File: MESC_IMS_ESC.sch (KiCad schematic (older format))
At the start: 58 parts, among them J1 Conn_01x08_Female, J2 Conn_01x08_Female, J3 Conn_01x08_Female, J4 Conn_01x06_Male, J5 Conn_ARM_JTAG_SWD_10, J6 USB_C_Receptacle_USB2.0, J7 Conn_01x03_Male, J8 Conn_01x04_Male, J9 Conn_01x08_Male, U1 STM32F303CBTx, Y1 ASE-8.000MHZ-LC-T

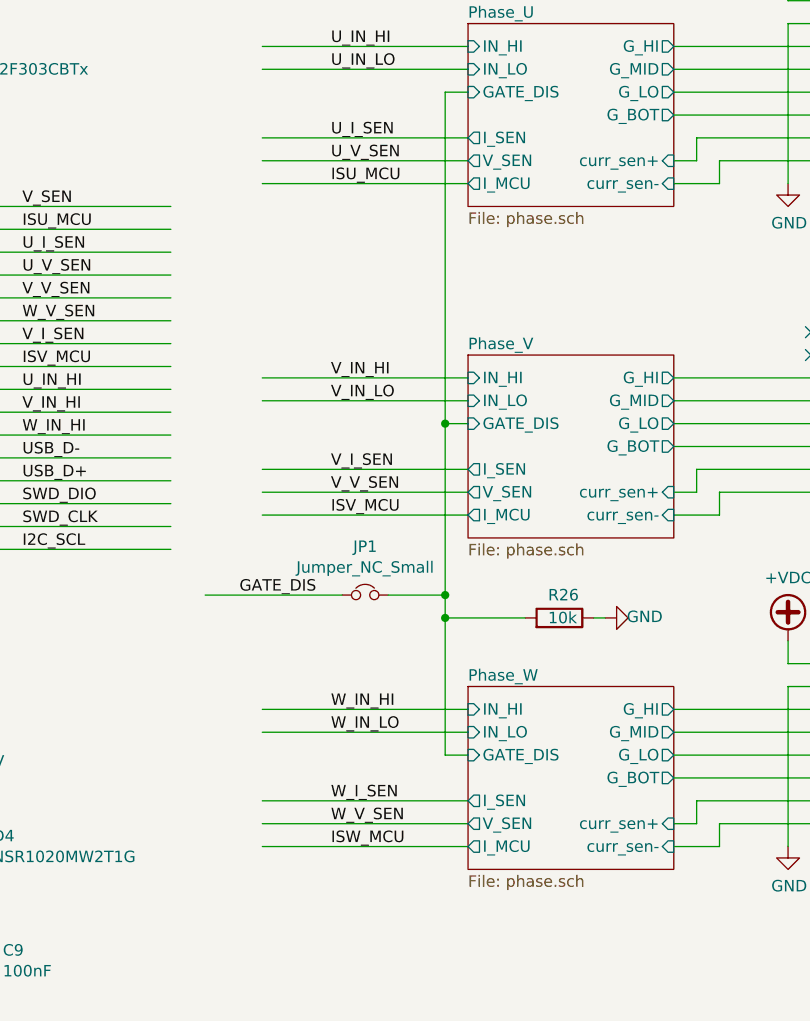
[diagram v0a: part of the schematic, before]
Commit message: Minor updates
Tweaking the README.md
Removing F303 op-amp circuitry.
Re-arranging INA240 circuit
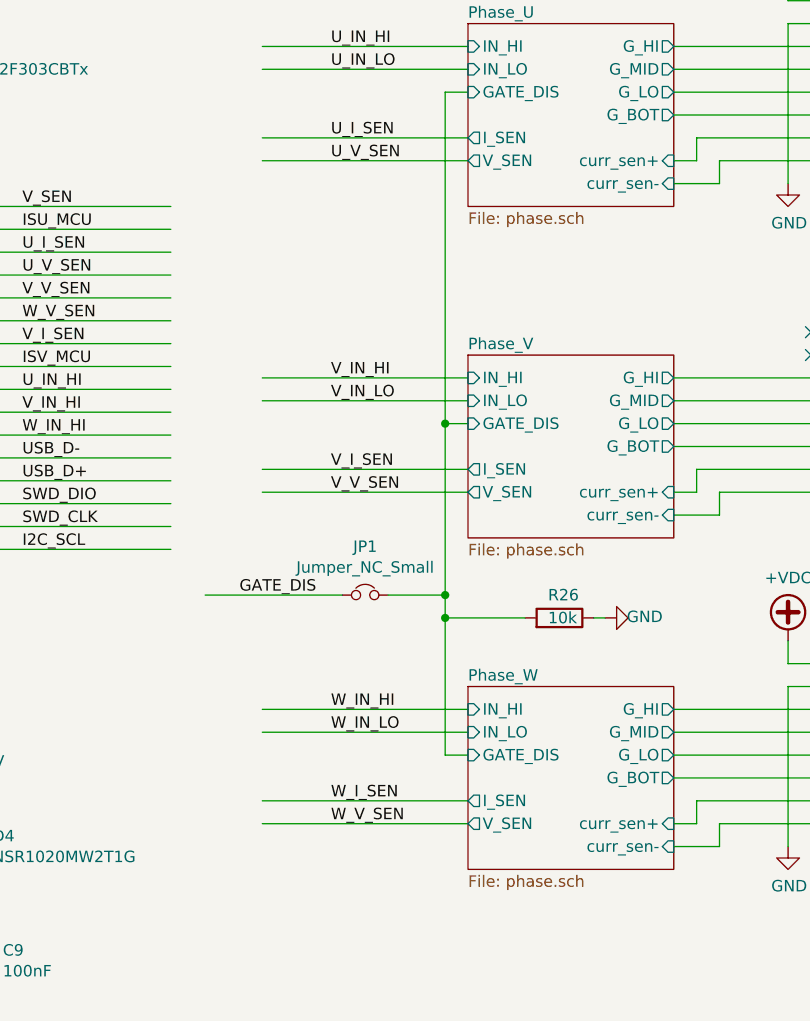
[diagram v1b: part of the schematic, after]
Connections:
- wire segments 279 -> 276
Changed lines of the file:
@@
 F11 "G_BOT" O R 9550 2950 50
 F12 "GATE_DIS" I L 8650 2850 50
-F13 "I_MCU" O L 8650 3250 50
 $EndSheet
 $Sheet
@@
 F11 "G_BOT" O R 9550 4400 50
 F12 "GATE_DIS" I L 8650 4300 50
-F13 "I_MCU" O L 8650 4700 50
 $EndSheet
 $Sheet
@@
 F11 "G_BOT" O R 9550 5850 50
 F12 "GATE_DIS" I L 8650 5750 50
-F13 "I_MCU" O L 8650 6150 50
 $EndSheet
 Wire Wire Line
@@
 	10050 2250 10050 2350
 Wire Wire Line
-	8650 3250 7750 3250
-Text Label 8050 3250 0    50   ~ 0
-ISU_MCU
-Wire Wire Line
 	5150 3850 4250 3850
 Text Label 4500 3850 0    50   ~ 0
 GATE_DIS
 Wire Wire Line
-	8650 4700 7750 4700
-Text Label 8050 4700 0    50   ~ 0
-ISV_MCU
-Wire Wire Line
-	8650 6150 7750 6150
-Text Label 8050 6150 0    50   ~ 0
-ISW_MCU
-Wire Wire Line
 	8650 2850 8550 2850

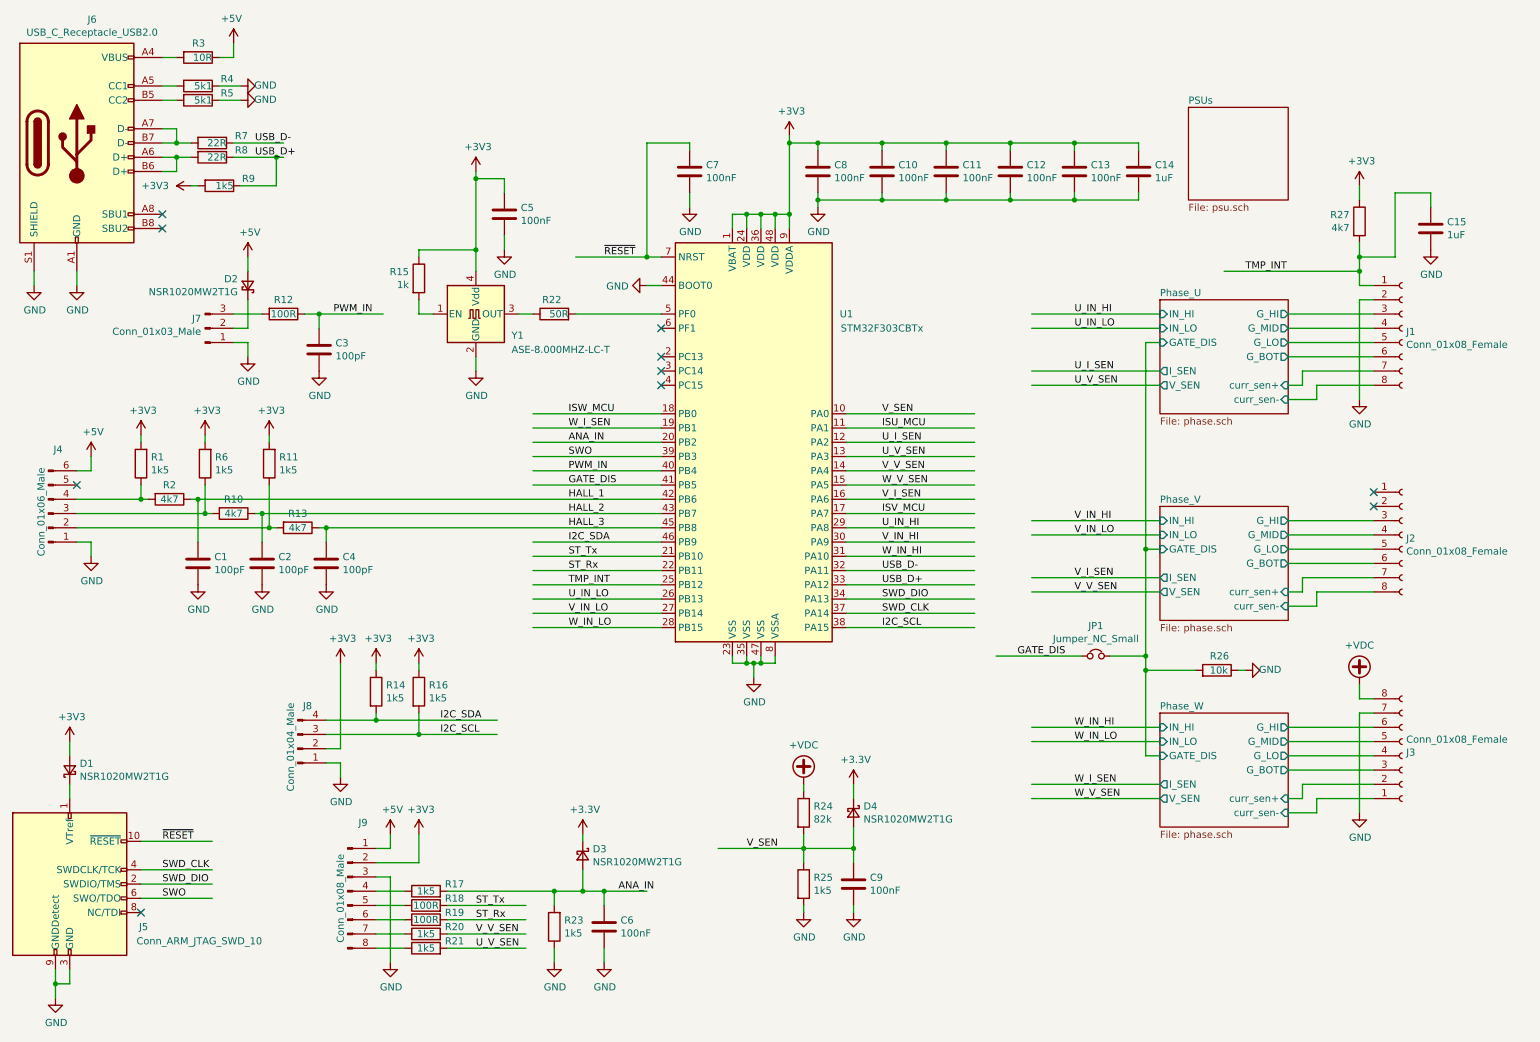
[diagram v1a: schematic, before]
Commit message: Adding some test points
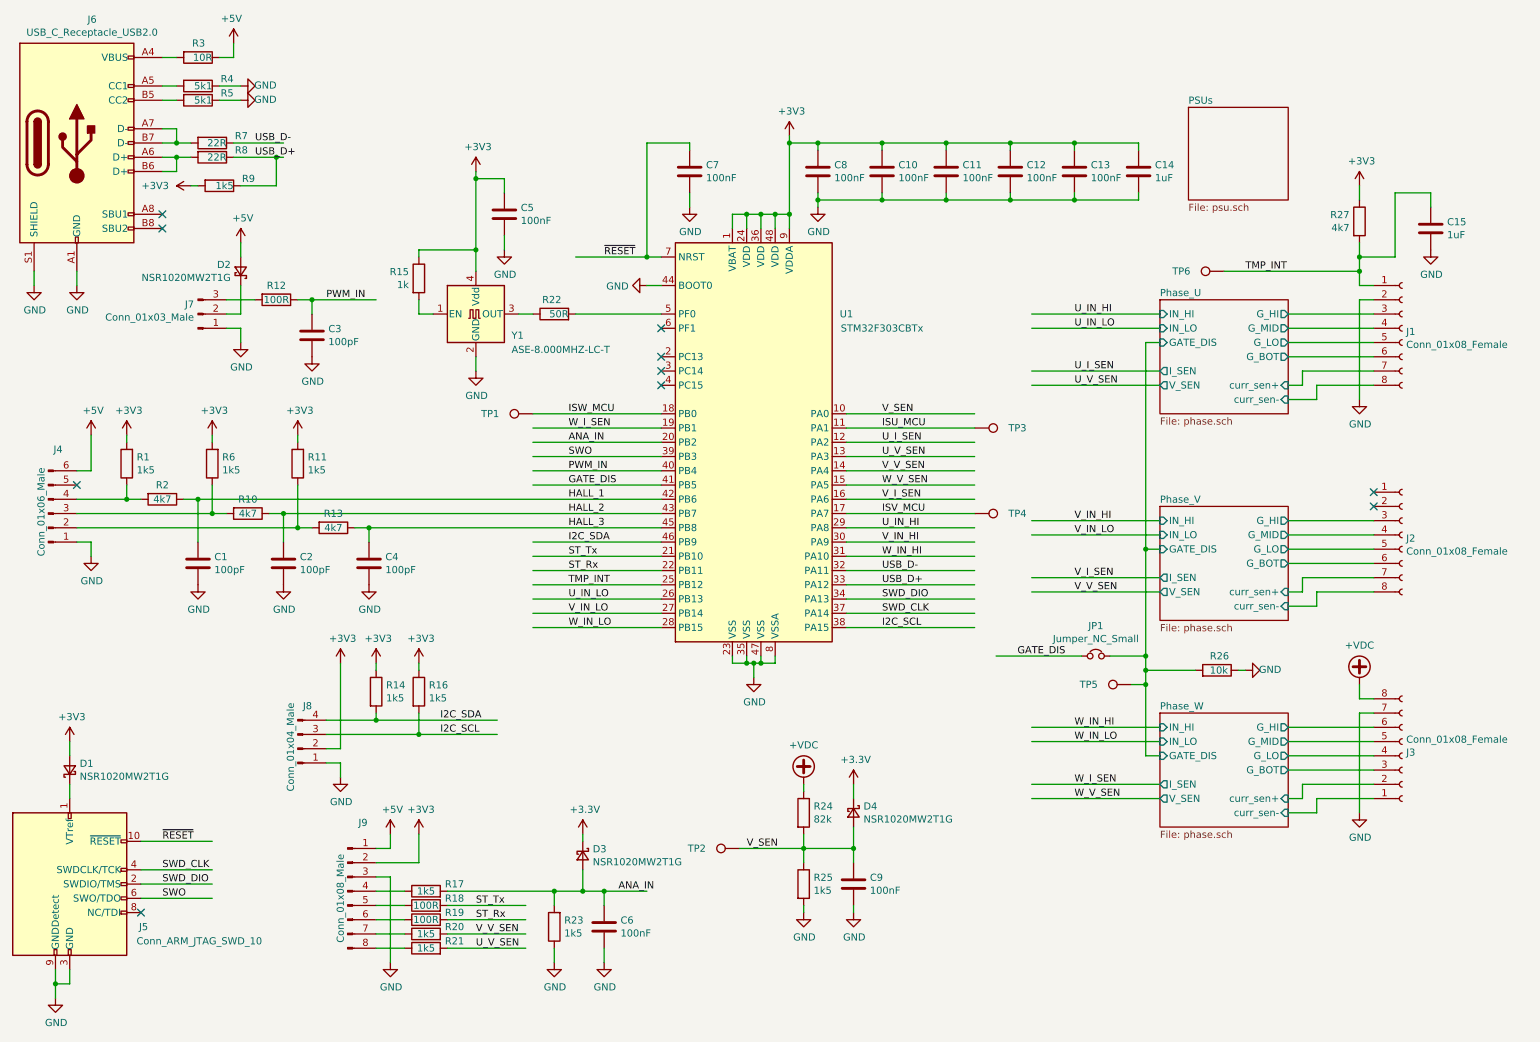
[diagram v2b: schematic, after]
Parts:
- added TP1, TP2, TP3, TP4, TP5, TP6: TestPoint, symbol Connector:TestPoint
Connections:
- wire segments 276 -> 278
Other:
- moved on the sheet: C2, C3, C4, D2, J7, R1, R10, R11, R12, R13, R2, R6

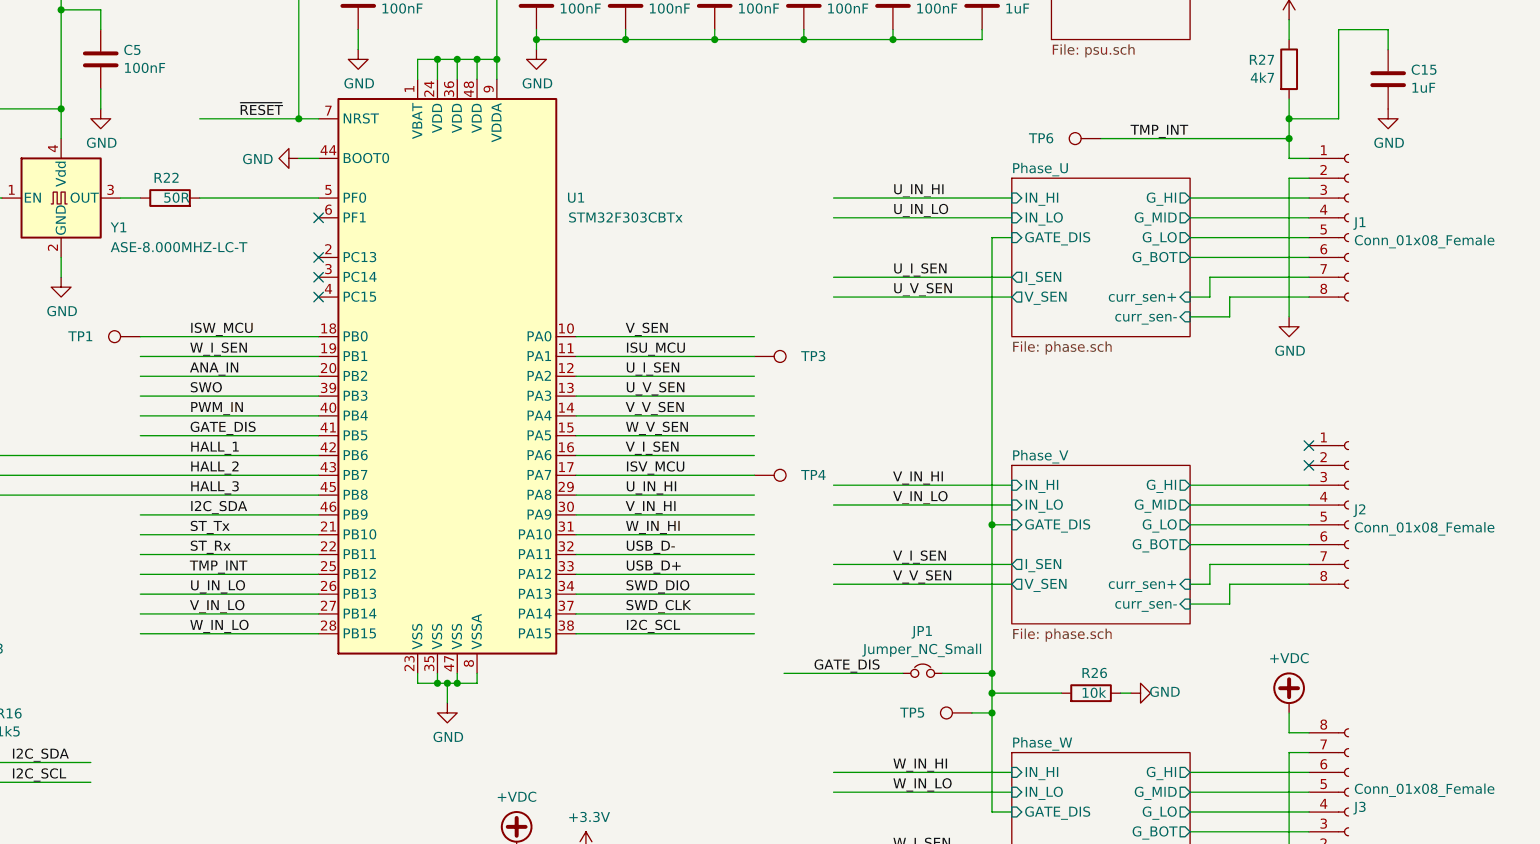
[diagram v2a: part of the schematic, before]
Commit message: Assigned all footprints
Began initial placement
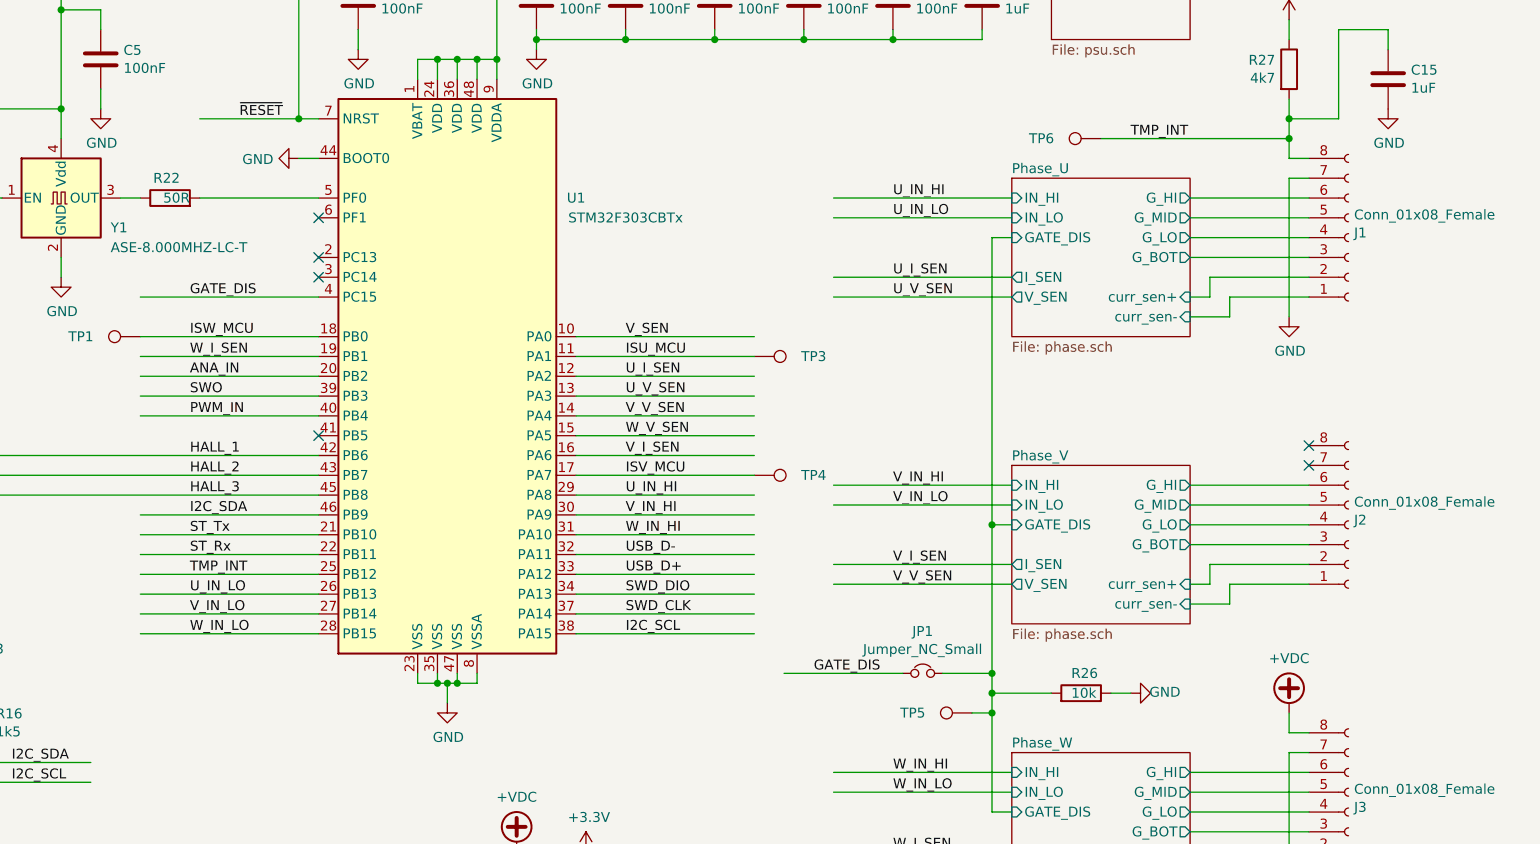
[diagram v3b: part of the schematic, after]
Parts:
- C14: footprint (none) -> Capacitor_SMD:C_0402_1005Metric
- TP1, TP2, TP3, TP4, TP5, TP6: footprint (none) -> TestPoint:TestPoint_Pad_D1.5mm
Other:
- moved on the sheet: R26
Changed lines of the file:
@@
 L Connector:Conn_01x08_Female J1
 U 1 1 607F595D
-P 10350 2750
-F 0 "J1" H 10378 2726 50  0000 L CNN
-F 1 "Conn_01x08_Female" H 10378 2635 50  0000 L CNN
-F 2 "Connector_PinSocket_2.54mm:PinSocket_1x08_P2.54mm_Horizontal" H 10350 2750 50  0001 C CNN
-F 3 "~" H 10350 2750 50  0001 C CNN
-	1    10350 2750
-	1    0    0    -1
+P 10350 2850
+F 0 "J1" H 10378 2826 50  0000 L CNN
+F 1 "Conn_01x08_Female" H 10378 2735 50  0000 L CNN
+F 2 "Connector_PinSocket_2.54mm:PinSocket_1x08_P2.54mm_Horizontal" H 10350 2850 50  0001 C CNN
+F 3 "~" H 10350 2850 50  0001 C CNN
+	1    10350 2850
+	1    0    0    1
 $EndComp
 $Comp
 L Connector:Conn_01x08_Female J2
 U 1 1 607F7758
-P 10350 4200
-F 0 "J2" H 10378 4176 50  0000 L CNN
-F 1 "Conn_01x08_Female" H 10378 4085 50  0000 L CNN
-F 2 "Connector_PinSocket_2.54mm:PinSocket_1x08_P2.54mm_Horizontal" H 10350 4200 50  0001 C CNN
-F 3 "~" H 10350 4200 50  0001 C CNN
-	1    10350 4200
-	1    0    0    -1
+P 10350 4300
+F 0 "J2" H 10378 4276 50  0000 L CNN
+F 1 "Conn_01x08_Female" H 10378 4185 50  0000 L CNN
+F 2 "Connector_PinSocket_2.54mm:PinSocket_1x08_P2.54mm_Horizontal" H 10350 4300 50  0001 C CNN
+F 3 "~" H 10350 4300 50  0001 C CNN
+	1    10350 4300
+	1    0    0    1
 $EndComp
 $Comp
@@
 NoConn ~ 5150 2950
 NoConn ~ 5150 3050
-NoConn ~ 5150 3150
 NoConn ~ 1500 6850
 Wire Wire Line
@@
 F 0 "C14" H 8615 1696 50  0000 L CNN
 F 1 "1uF" H 8615 1605 50  0000 L CNN
-F 2 "" H 8538 1500 50  0001 C CNN
+F 2 "Capacitor_SMD:C_0402_1005Metric" H 8538 1500 50  0001 C CNN
 F 3 "~" H 8500 1650 50  0001 C CNN
 	1    8500 1650
@@
 	10050 2250 10050 2350
 Wire Wire Line
-	5150 3850 4250 3850
-Text Label 4500 3850 0    50   ~ 0
+	5150 3150 4250 3150
+Text Label 4500 3150 0    50   ~ 0
 GATE_DIS
 Wire Wire Line
@@
 $EndComp
 Wire Wire Line
-	9200 5150 9250 5150
+	9150 5150 9250 5150
 $Comp
 L Device:R R?
 U 1 1 61980155
-P 9050 5150
+P 9000 5150
 AR Path="/6070CE7F/61980155" Ref="R?"  Part="1"
 AR Path="/6074FE4E/61980155" Ref="R?"  Part="1"
 AR Path="/6075047A/61980155" Ref="R?"  Part="1"
 AR Path="/61980155" Ref="R26"  Part="1"
-F 0 "R26" V 9150 5100 50  0000 L CNN
-F 1 "10k" V 9050 5100 50  0000 L CNN
-F 2 "Resistor_SMD:R_0402_1005Metric" V 8980 5150 50  0001 C CNN
-F 3 "~" H 9050 5150 50  0001 C CNN
-	1    9050 5150
+F 0 "R26" V 9100 5100 50  0000 L CNN
+F 1 "10k" V 9000 5100 50  0000 L CNN
+F 2 "Resistor_SMD:R_0402_1005Metric" V 8930 5150 50  0001 C CNN
+F 3 "~" H 9000 5150 50  0001 C CNN
+	1    9000 5150
 	0    1    -1   0
 $EndComp
@@
 	8550 4300 8550 5050
 Wire Wire Line
-	8900 5150 8550 5150
+	8850 5150 8550 5150
 Wire Wire Line
 	8550 2850 8550 4300
@@
 F 0 "TP1" V 4250 3650 50  0000 C CNN
 F 1 "TestPoint" V 4354 3422 50  0001 C CNN
-F 2 "" H 4450 3350 50  0001 C CNN
+F 2 "TestPoint:TestPoint_Pad_D1.5mm" H 4450 3350 50  0001 C CNN
 F 3 "~" H 4450 3350 50  0001 C CNN
 	1    4250 3350
@@
 F 0 "TP3" V 7350 3750 50  0000 C CNN
 F 1 "TestPoint" V 7454 3522 50  0001 C CNN
-F 2 "" H 7550 3450 50  0001 C CNN
+F 2 "TestPoint:TestPoint_Pad_D1.5mm" H 7550 3450 50  0001 C CNN
 F 3 "~" H 7550 3450 50  0001 C CNN
 	1    7350 3450
@@
 F 0 "TP4" V 7350 4350 50  0000 C CNN
 F 1 "TestPoint" V 7454 4122 50  0001 C CNN
-F 2 "" H 7550 4050 50  0001 C CNN
+F 2 "TestPoint:TestPoint_Pad_D1.5mm" H 7550 4050 50  0001 C CNN
 F 3 "~" H 7550 4050 50  0001 C CNN
 	1    7350 4050
@@
 F 0 "TP6" V 9100 2650 50  0000 C CNN
 F 1 "TestPoint" V 9204 2422 50  0001 C CNN
-F 2 "" H 9300 2350 50  0001 C CNN
+F 2 "TestPoint:TestPoint_Pad_D1.5mm" H 9300 2350 50  0001 C CNN
 F 3 "~" H 9300 2350 50  0001 C CNN
 	1    9100 2350
@@
 F 0 "TP2" V 5700 6700 50  0000 C CNN
 F 1 "TestPoint" V 5804 6472 50  0001 C CNN
-F 2 "" H 5900 6400 50  0001 C CNN
+F 2 "TestPoint:TestPoint_Pad_D1.5mm" H 5900 6400 50  0001 C CNN
 F 3 "~" H 5900 6400 50  0001 C CNN
 	1    5700 6400
@@
 F 0 "TP5" V 8450 5550 50  0000 C CNN
 F 1 "TestPoint" V 8554 5322 50  0001 C CNN
-F 2 "" H 8650 5250 50  0001 C CNN
+F 2 "TestPoint:TestPoint_Pad_D1.5mm" H 8650 5250 50  0001 C CNN
 F 3 "~" H 8650 5250 50  0001 C CNN
 	1    8450 5250
@@
 Wire Wire Line
 	8550 5250 8550 5750
+NoConn ~ 5150 3850
 $EndSCHEMATC
